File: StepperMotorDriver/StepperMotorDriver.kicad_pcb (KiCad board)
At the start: 2 copper layers, 1 part, among them U1 A4988SETTR-T

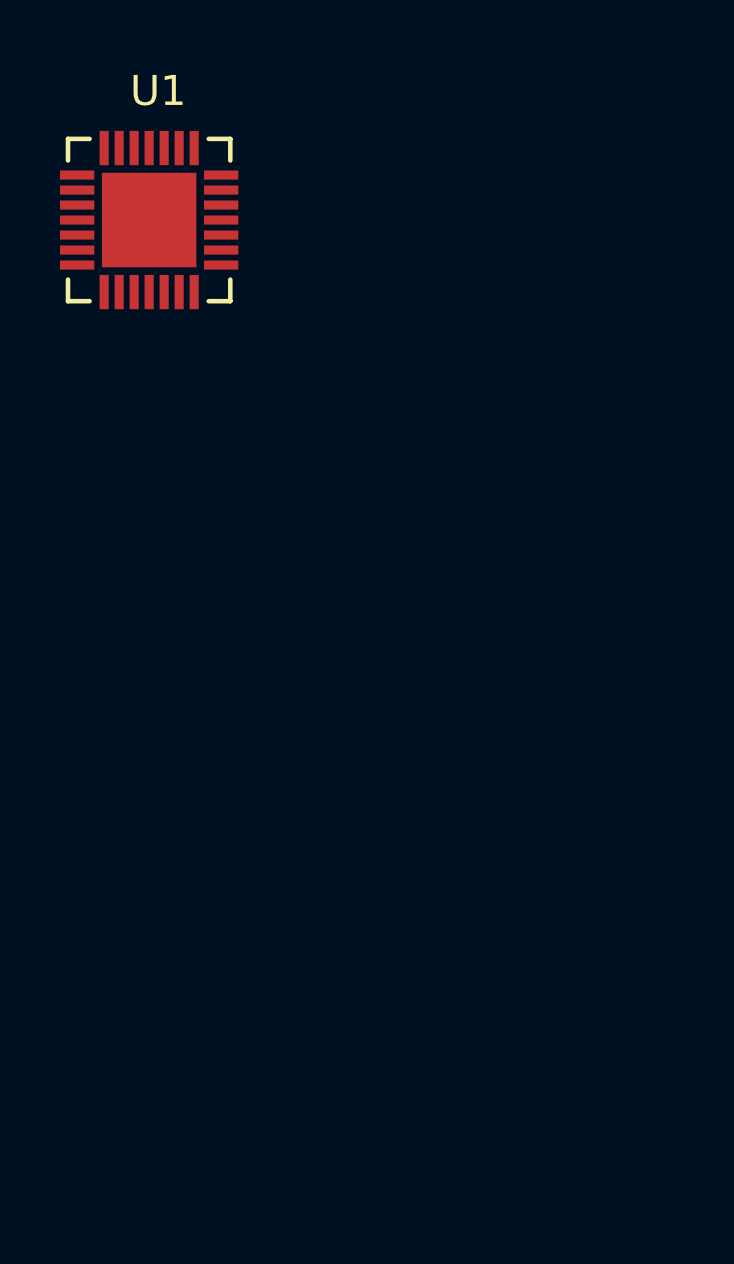
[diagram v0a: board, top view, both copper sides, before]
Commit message: changed schematic, assigned footprints
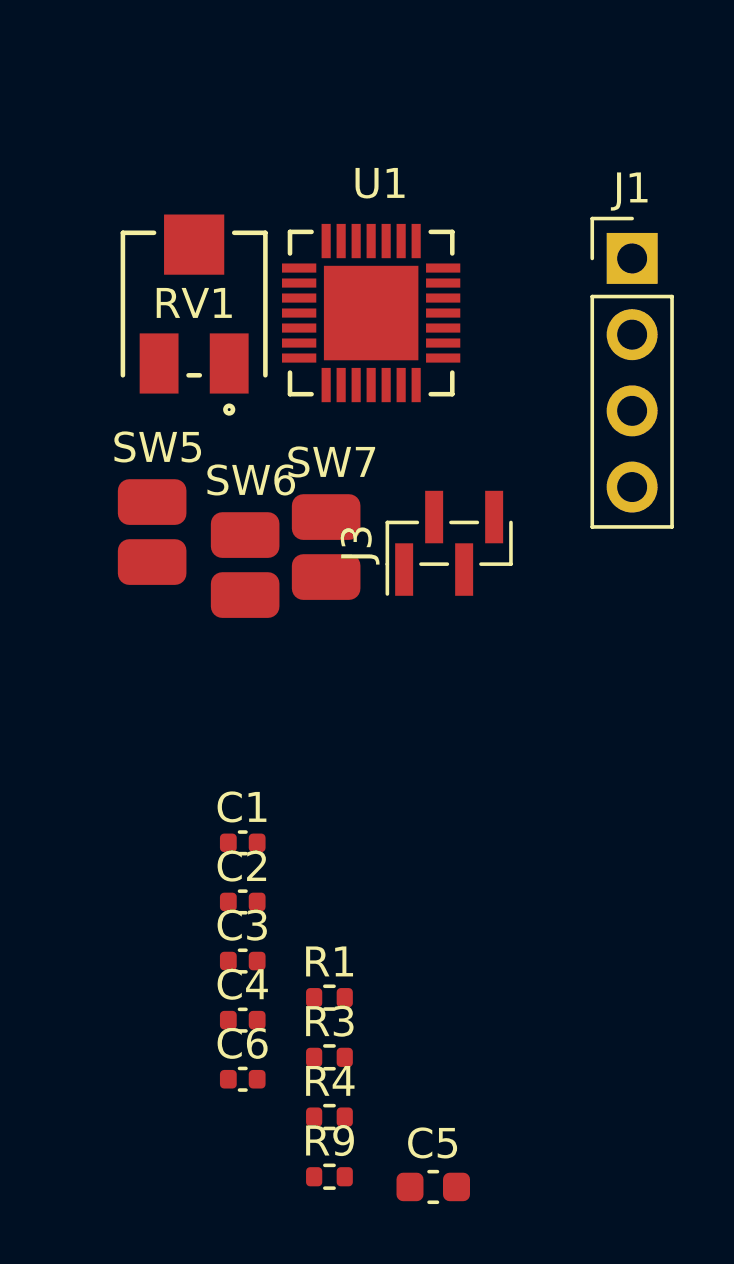
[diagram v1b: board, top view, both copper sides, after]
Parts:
- added C1: 0.22u, Capacitor_SMD:C_0402_1005Metric, F.Cu at (155.8, 122.9)
- added C2: 0.1u, Capacitor_SMD:C_0402_1005Metric, F.Cu at (155.8, 124.8)
- added C3: 0.1u, Capacitor_SMD:C_0402_1005Metric, F.Cu at (155.8, 126.8)
- added C4: 0.22u, Capacitor_SMD:C_0402_1005Metric, F.Cu at (155.8, 128.8)
- added C5: 4.7u, Capacitor_SMD:C_0603_1608Metric, F.Cu at (162.2, 134.3)
- added C6: 0.1u, Capacitor_SMD:C_0402_1005Metric, F.Cu at (155.8, 130.7)
- added J1: Conn_01x04_Pin, Connector_PinHeader_2.54mm:PinHeader_1x04_P2.54mm_Vertical, F.Cu at (168.8, 103.4)
- added J3: Conn_01x04_Pin, Connector_PinHeader_1.00mm:PinHeader_1x04_P1.00mm_Vertical_SMD_Pin1Left, F.Cu at (162.7, 112.9)
- added R1: 5k, Resistor_SMD:R_0402_1005Metric, F.Cu at (158.7, 128.0)
- added R3: 68m, Resistor_SMD:R_0402_1005Metric, F.Cu at (158.7, 130.0)
- added R4: 68m, Resistor_SMD:R_0402_1005Metric, F.Cu at (158.7, 132.0)
- added R9: 10k, Resistor_SMD:R_0402_1005Metric, F.Cu at (158.7, 134.0)
- added RV1: 10k, Footprints:POT_3314J, F.Cu at (154.2, 104.9)
- added SW5: SW_Push, Footprints:Pads to short, F.Cu at (152.0, 110.7)
- added SW6: SW_Push, Footprints:Pads to short, F.Cu at (155.1, 111.8)
- added SW7: SW_Push, Footprints:Pads to short, F.Cu at (157.8, 111.2)
- moved U1 8.02 mm to (160.1, 105.2)
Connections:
- U1 pad 1: unconnected-(U1-OUT2B-Pad1) -> Net-(J1-Pin_4)
- U1 pad 10: unconnected-(U1-MS2-Pad10) -> /MS2
- U1 pad 11: unconnected-(U1-MS3-Pad11) -> /MS3
- U1 pad 12: unconnected-(U1-~{RESET}-Pad12) -> Net-(J3-Pin_2)
- U1 pad 13: Net-(U1-ROSC) -> GND
- U1 pad 16: unconnected-(U1-STEP-Pad16) -> Net-(J3-Pin_3)
- U1 pad 17: unconnected-(U1-REF-Pad17) -> /V_{REF}
- U1 pad 19: unconnected-(U1-DIR-Pad19) -> Net-(J3-Pin_4)
- U1 pad 2: unconnected-(U1-~{ENABLE}-Pad2) -> Net-(J3-Pin_1)
- U1 pad 21: unconnected-(U1-OUT1B-Pad21) -> Net-(J1-Pin_2)
- U1 pad 24: unconnected-(U1-OUT1A-Pad24) -> Net-(J1-Pin_1)
- U1 pad 26: unconnected-(U1-OUT2A-Pad26) -> Net-(J1-Pin_3)
- U1 pad 29: (no net) -> GND
- U1 pad 9: unconnected-(U1-MS1-Pad9) -> /MS1
